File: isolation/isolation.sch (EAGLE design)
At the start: 21 parts, among them IC1 XTLV61048DBVR

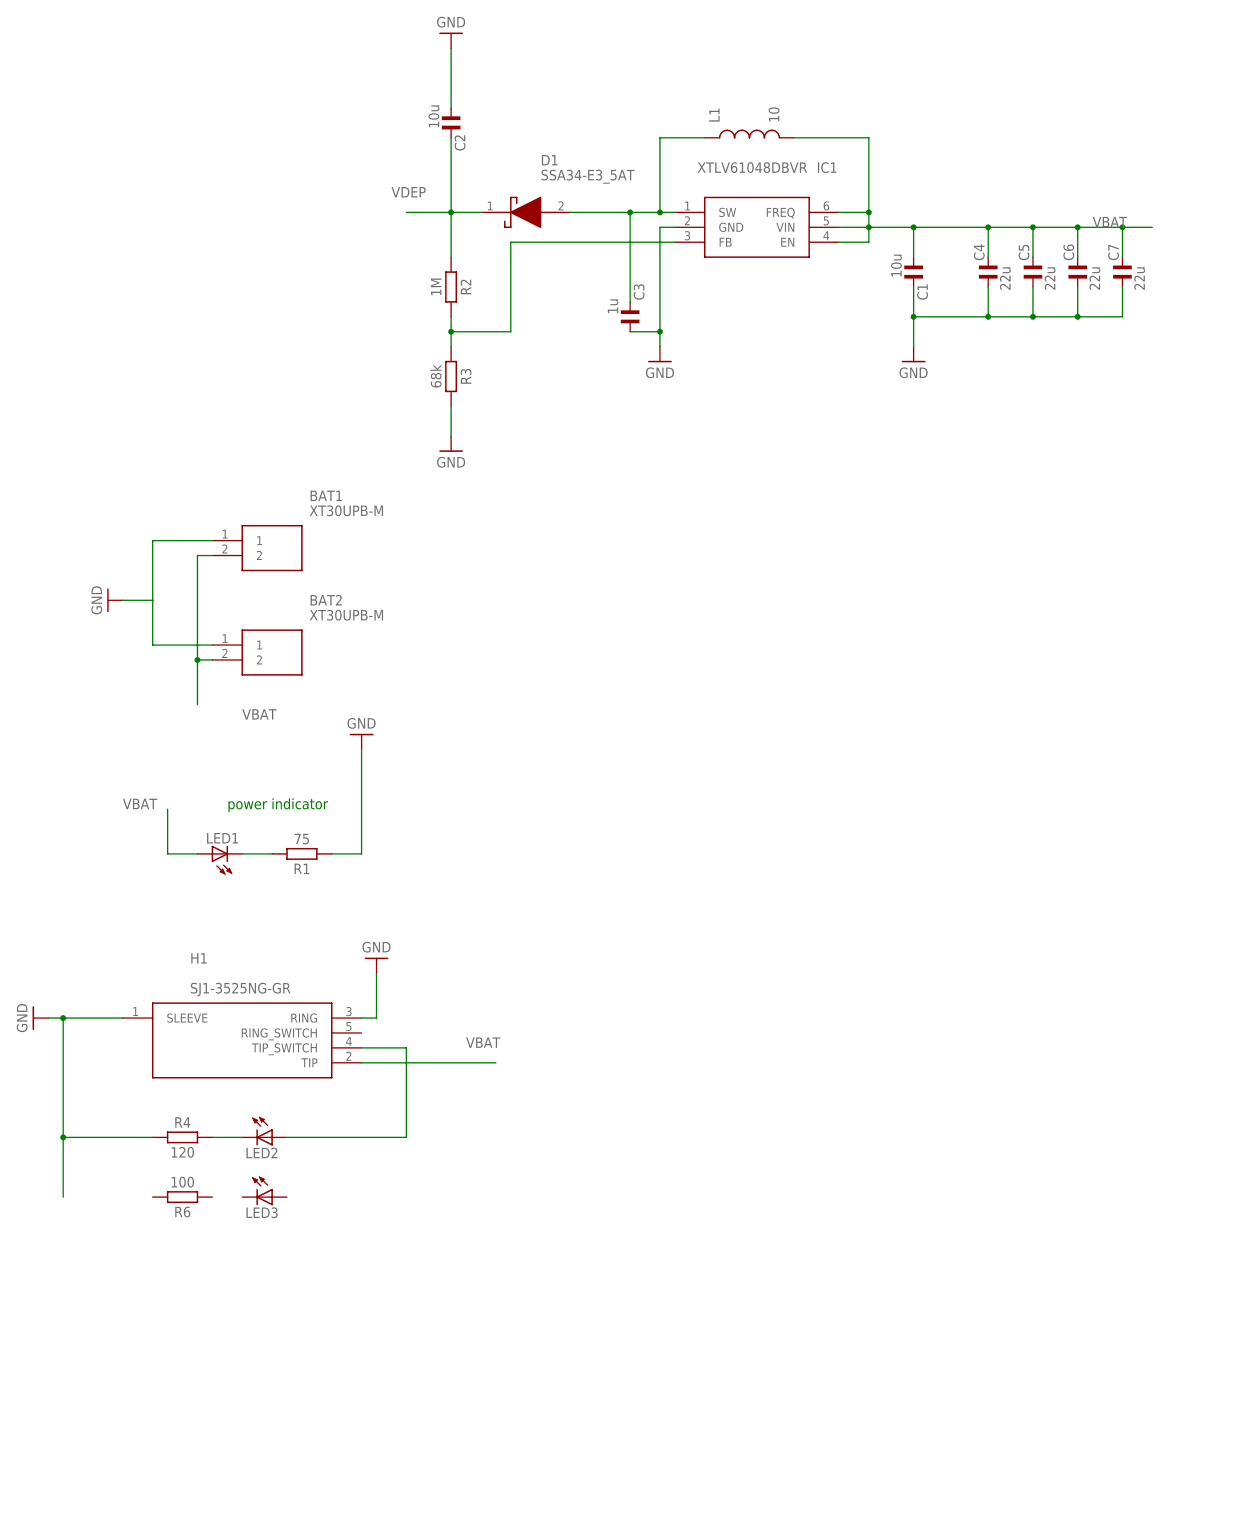
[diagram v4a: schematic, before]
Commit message: headphone jack with inverter
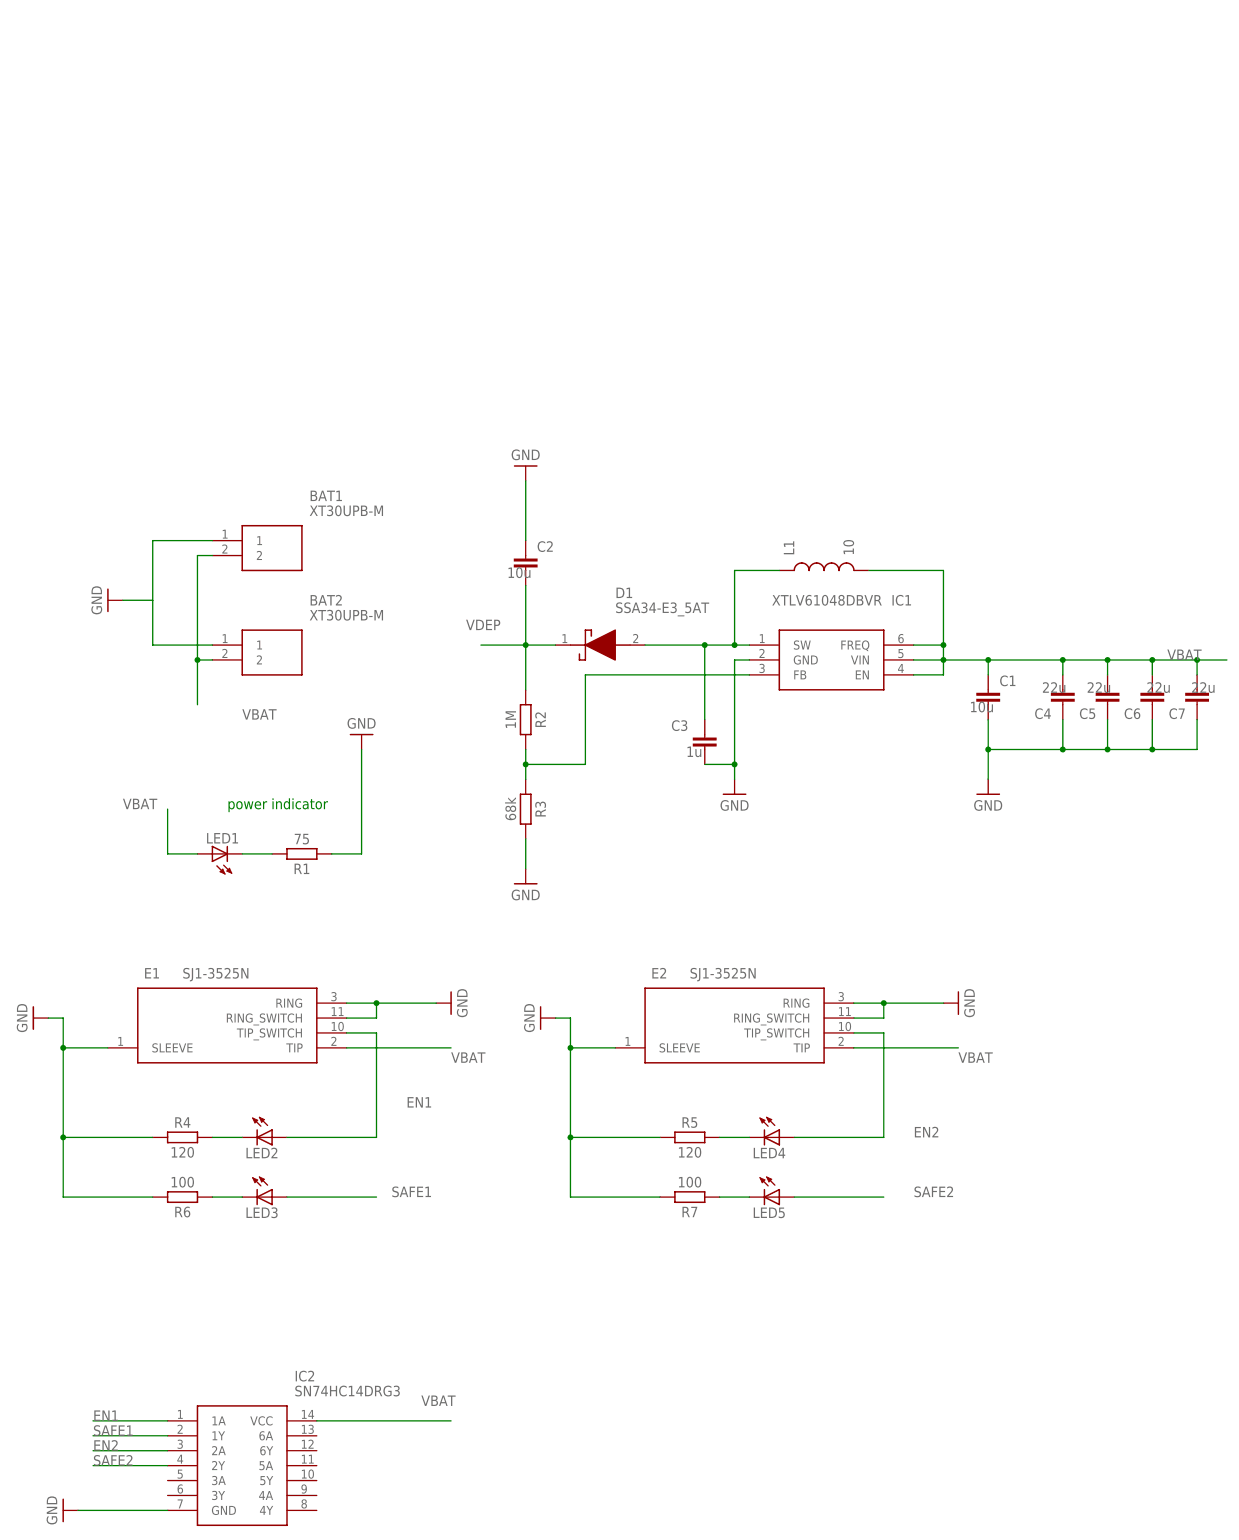
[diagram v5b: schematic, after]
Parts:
- removed H1: SJ1-3525NG-GR, SamacSys_Parts:SJ1-3525NG-GR
- added E1, E2: SJ1-3525N, SamacSys_Parts:SJ1-3525N
- added IC2: SN74HC14DRG3, SamacSys_Parts:SN74HC14DRG3
- added LED4, LED5: (no value), adafruit:LEDCHIPLED_0805
- added R5: 120, Resistor:R_CHIP-0603(1608-METRIC)
- added R7: 100, Resistor:R_CHIP-0603(1608-METRIC)
- C1, C2, C3, C4, C5, C6, C7: device 52101-101-REV-A_v16:RC-MASTER-SMD_C_0603MP -> Capacitor:C_CHIP-0603(1608-METRIC)
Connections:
- new net EN2: E2.TIP_SWITCH, IC2.2A, LED4.A
- new net N$4: LED4.C, R5.2
- new net N$6: LED3.C, R6.1
- new net N$7: LED5.C, R7.1
- new net SAFE1: IC2.1Y, LED3.A
- new net SAFE2: IC2.2Y, LED5.A
- net EN1: now also E1.TIP_SWITCH, IC2.1A; no longer H1.TIP_SWITCH
- net GND: now also E1.RING, E1.RING_SWITCH, E1.SLEEVE, E2.RING, E2.RING_SWITCH, E2.SLEEVE, IC2.GND, R5.1, R6.2, R7.2; no longer H1.RING, H1.SLEEVE
- net VBAT: now also E1.TIP, E2.TIP, IC2.VCC; no longer H1.TIP
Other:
- moved on the sheet: D1, IC1, L1, R2, R3

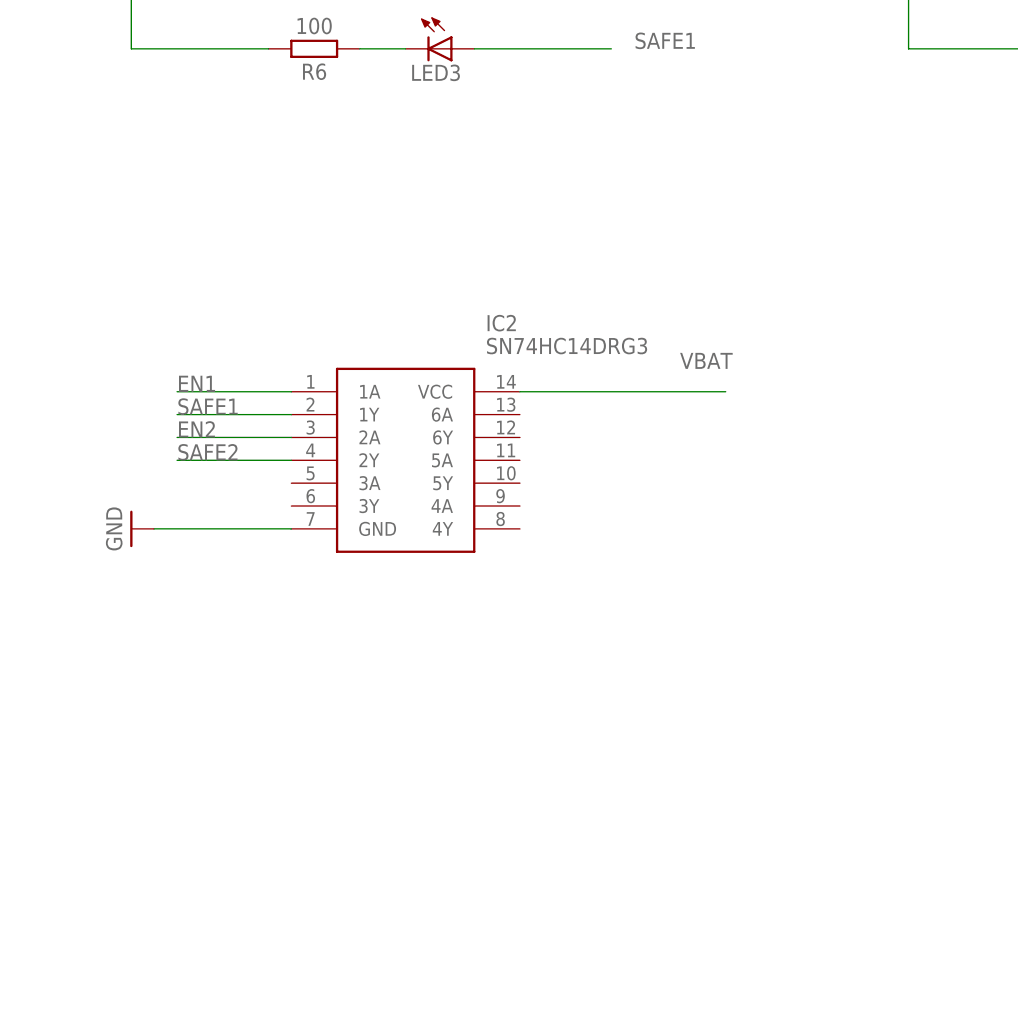
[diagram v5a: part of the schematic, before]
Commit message: jst inputs from flight computers
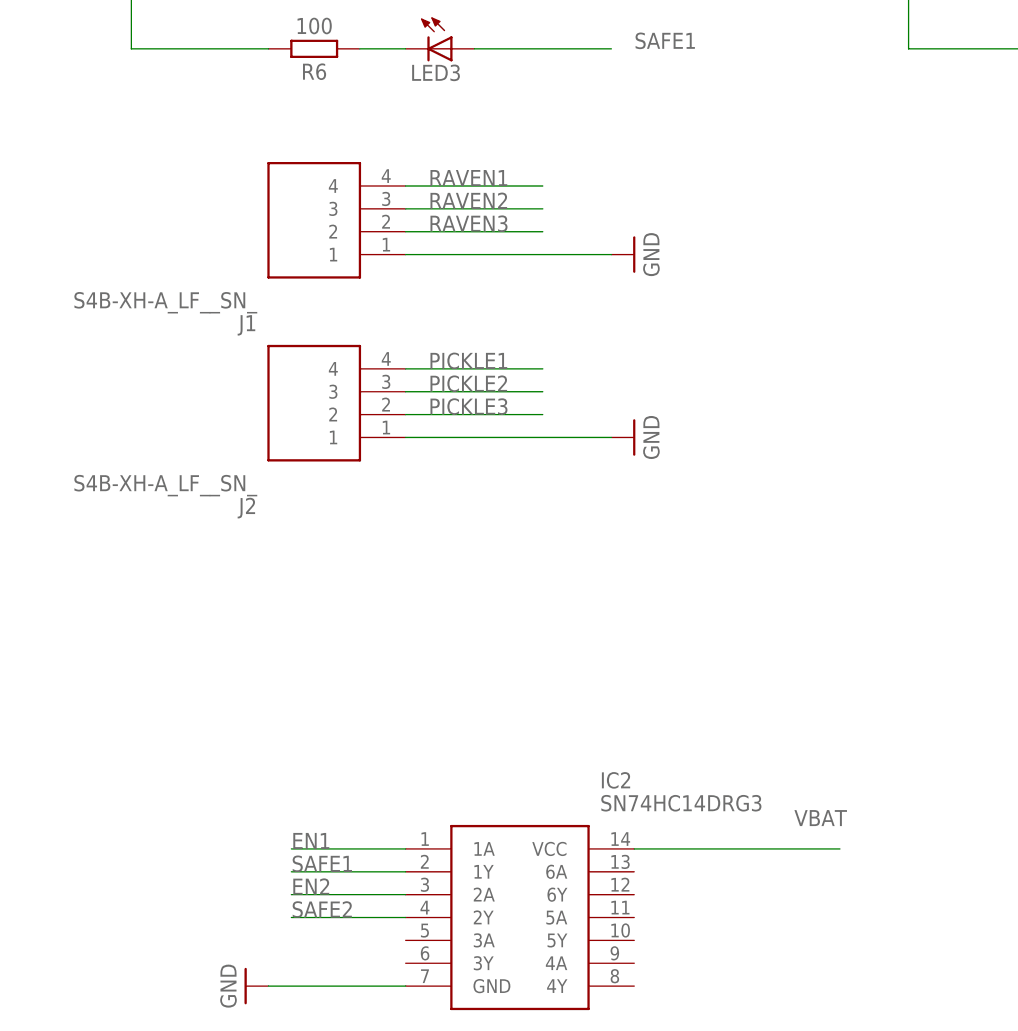
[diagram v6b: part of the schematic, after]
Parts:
- added J1, J2: S4B-XH-A_LF__SN_, SamacSys_Parts:S4B-XH-A_LF__SN_
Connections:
- new net PICKLE1: J2.4
- new net PICKLE2: J2.3
- new net PICKLE3: J2.2
- new net RAVEN1: J1.4
- new net RAVEN2: J1.3
- new net RAVEN3: J1.2
- net GND: now also J1.1, J2.1
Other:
- moved on the sheet: IC2
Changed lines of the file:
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@@
 <part name="E2" library="SamacSys_Parts" deviceset="SJ1-3525N" device=""/>
 <part name="SUPPLY11" library="Power_Symbols" library_urn="urn:adsk.eagle:library:16502351" deviceset="GND-BAR" device="" value="GND"/>
+<part name="J1" library="SamacSys_Parts" deviceset="S4B-XH-A_LF__SN_" device=""/>
+<part name="J2" library="SamacSys_Parts" deviceset="S4B-XH-A_LF__SN_" device=""/>
+<part name="SUPPLY12" library="Power_Symbols" library_urn="urn:adsk.eagle:library:16502351" deviceset="GND-BAR" device="" value="GND"/>
+<part name="SUPPLY13" library="Power_Symbols" library_urn="urn:adsk.eagle:library:16502351" deviceset="GND-BAR" device="" value="GND"/>
 </parts>
 <sheets>
@@
 <attribute name="VALUE" x="60.325" y="-27.94" size="1.778" layer="96" rot="R90" align="center"/>
 </instance>
-<instance part="IC2" gate="G$1" x="10.16" y="-99.06" smashed="yes">
-<attribute name="NAME" x="31.75" y="-91.44" size="1.778" layer="95" align="center-left"/>
-<attribute name="VALUE" x="31.75" y="-93.98" size="1.778" layer="96" align="center-left"/>
-</instance>
-<instance part="SUPPLY9" gate="G$1" x="-7.62" y="-114.3" smashed="yes" rot="R270">
-<attribute name="VALUE" x="-9.525" y="-114.3" size="1.778" layer="96" rot="R270" align="center"/>
+<instance part="IC2" gate="G$1" x="22.86" y="-149.86" smashed="yes">
+<attribute name="NAME" x="44.45" y="-142.24" size="1.778" layer="95" align="center-left"/>
+<attribute name="VALUE" x="44.45" y="-144.78" size="1.778" layer="96" align="center-left"/>
+</instance>
+<instance part="SUPPLY9" gate="G$1" x="5.08" y="-165.1" smashed="yes" rot="R270">
+<attribute name="VALUE" x="3.175" y="-165.1" size="1.778" layer="96" rot="R270" align="center"/>
 </instance>
 <instance part="SUPPLY10" gate="G$1" x="73.66" y="-30.48" smashed="yes" rot="R270">
@@
 <instance part="SUPPLY11" gate="G$1" x="144.78" y="-27.94" smashed="yes" rot="R90">
 <attribute name="VALUE" x="146.685" y="-27.94" size="1.778" layer="96" rot="R90" align="center"/>
+</instance>
+<instance part="J1" gate="G$1" x="22.86" y="-83.82" smashed="yes" rot="R180">
+<attribute name="NAME" x="6.35" y="-91.44" size="1.778" layer="95" rot="R180" align="center-left"/>
+<attribute name="VALUE" x="6.35" y="-88.9" size="1.778" layer="96" rot="R180" align="center-left"/>
+</instance>
+<instance part="J2" gate="G$1" x="22.86" y="-104.14" smashed="yes" rot="R180">
+<attribute name="NAME" x="6.35" y="-111.76" size="1.778" layer="95" rot="R180" align="center-left"/>
+<attribute name="VALUE" x="6.35" y="-109.22" size="1.778" layer="96" rot="R180" align="center-left"/>
+</instance>
+<instance part="SUPPLY12" gate="G$1" x="48.26" y="-104.14" smashed="yes" rot="R90">
+<attribute name="VALUE" x="50.165" y="-104.14" size="1.778" layer="96" rot="R90" align="center"/>
+</instance>
+<instance part="SUPPLY13" gate="G$1" x="48.26" y="-83.82" smashed="yes" rot="R90">
+<attribute name="VALUE" x="50.165" y="-83.82" size="1.778" layer="96" rot="R90" align="center"/>
 </instance>
 </instances>
@@
 <pinref part="IC2" gate="G$1" pin="GND"/>
 <pinref part="SUPPLY9" gate="G$1" pin="GND"/>
-<wire x1="10.16" y1="-114.3" x2="-5.08" y2="-114.3" width="0.1524" layer="91"/>
+<wire x1="22.86" y1="-165.1" x2="7.62" y2="-165.1" width="0.1524" layer="91"/>
 </segment>
 <segment>
@@
 <wire x1="132.08" y1="-30.48" x2="132.08" y2="-27.94" width="0.1524" layer="91"/>
 <junction x="132.08" y="-27.94"/>
+</segment>
+<segment>
+<pinref part="J1" gate="G$1" pin="1"/>
+<wire x1="22.86" y1="-83.82" x2="45.72" y2="-83.82" width="0.1524" layer="91"/>
+<pinref part="SUPPLY13" gate="G$1" pin="GND"/>
+</segment>
+<segment>
+<pinref part="J2" gate="G$1" pin="1"/>
+<wire x1="22.86" y1="-104.14" x2="45.72" y2="-104.14" width="0.1524" layer="91"/>
+<pinref part="SUPPLY12" gate="G$1" pin="GND"/>
 </segment>
 </net>
@@
 <segment>
 <pinref part="IC2" gate="G$1" pin="VCC"/>
-<wire x1="35.56" y1="-99.06" x2="58.42" y2="-99.06" width="0.1524" layer="91"/>
-<label x="53.34" y="-96.52" size="1.778" layer="95"/>
+<wire x1="48.26" y1="-149.86" x2="71.12" y2="-149.86" width="0.1524" layer="91"/>
+<label x="66.04" y="-147.32" size="1.778" layer="95"/>
 </segment>
 <segment>
@@
 <segment>
 <pinref part="IC2" gate="G$1" pin="1A"/>
-<wire x1="10.16" y1="-99.06" x2="-2.54" y2="-99.06" width="0.1524" layer="91"/>
-<label x="-2.54" y="-99.06" size="1.778" layer="95"/>
+<wire x1="22.86" y1="-149.86" x2="10.16" y2="-149.86" width="0.1524" layer="91"/>
+<label x="10.16" y="-149.86" size="1.778" layer="95"/>
 </segment>
 </net>
@@
 <segment>
 <pinref part="IC2" gate="G$1" pin="1Y"/>
-<wire x1="10.16" y1="-101.6" x2="-2.54" y2="-101.6" width="0.1524" layer="91"/>
-<label x="-2.54" y="-101.6" size="1.778" layer="95"/>
+<wire x1="22.86" y1="-152.4" x2="10.16" y2="-152.4" width="0.1524" layer="91"/>
+<label x="10.16" y="-152.4" size="1.778" layer="95"/>
 </segment>
 <segment>
@@
 <segment>
 <pinref part="IC2" gate="G$1" pin="2A"/>
-<wire x1="10.16" y1="-104.14" x2="-2.54" y2="-104.14" width="0.1524" layer="91"/>
-<label x="-2.54" y="-104.14" size="1.778" layer="95"/>
+<wire x1="22.86" y1="-154.94" x2="10.16" y2="-154.94" width="0.1524" layer="91"/>
+<label x="10.16" y="-154.94" size="1.778" layer="95"/>
 </segment>
 <segment>
@@
 <segment>
 <pinref part="IC2" gate="G$1" pin="2Y"/>
-<wire x1="10.16" y1="-106.68" x2="-2.54" y2="-106.68" width="0.1524" layer="91"/>
-<label x="-2.54" y="-106.68" size="1.778" layer="95"/>
+<wire x1="22.86" y1="-157.48" x2="10.16" y2="-157.48" width="0.1524" layer="91"/>
+<label x="10.16" y="-157.48" size="1.778" layer="95"/>
 </segment>
 <segment>
@@
 </segment>
 </net>
+<net name="PICKLE3" class="0">
+<segment>
+<pinref part="J2" gate="G$1" pin="2"/>
+<wire x1="22.86" y1="-101.6" x2="38.1" y2="-101.6" width="0.1524" layer="91"/>
+<label x="25.4" y="-101.6" size="1.778" layer="95"/>
+</segment>
+</net>
+<net name="PICKLE2" class="0">
+<segment>
+<pinref part="J2" gate="G$1" pin="3"/>
+<wire x1="22.86" y1="-99.06" x2="38.1" y2="-99.06" width="0.1524" layer="91"/>
+<label x="25.4" y="-99.06" size="1.778" layer="95"/>
+</segment>
+</net>
+<net name="PICKLE1" class="0">
+<segment>
+<pinref part="J2" gate="G$1" pin="4"/>
+<wire x1="22.86" y1="-96.52" x2="38.1" y2="-96.52" width="0.1524" layer="91"/>
+<label x="25.4" y="-96.52" size="1.778" layer="95"/>
+</segment>
+</net>
+<net name="RAVEN3" class="0">
+<segment>
+<pinref part="J1" gate="G$1" pin="2"/>
+<wire x1="22.86" y1="-81.28" x2="38.1" y2="-81.28" width="0.1524" layer="91"/>
+<label x="25.4" y="-81.28" size="1.778" layer="95"/>
+</segment>
+</net>
+<net name="RAVEN2" class="0">
+<segment>
+<pinref part="J1" gate="G$1" pin="3"/>
+<wire x1="22.86" y1="-78.74" x2="38.1" y2="-78.74" width="0.1524" layer="91"/>
+<label x="25.4" y="-78.74" size="1.778" layer="95"/>
+</segment>
+</net>
+<net name="RAVEN1" class="0">
+<segment>
+<pinref part="J1" gate="G$1" pin="4"/>
+<wire x1="22.86" y1="-76.2" x2="38.1" y2="-76.2" width="0.1524" layer="91"/>
+<label x="25.4" y="-76.2" size="1.778" layer="95"/>
+</segment>
+</net>

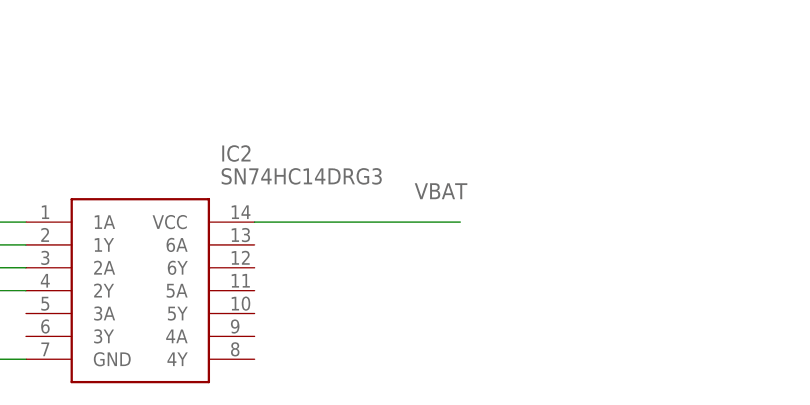
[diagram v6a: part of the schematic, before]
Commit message: invert raven inputs
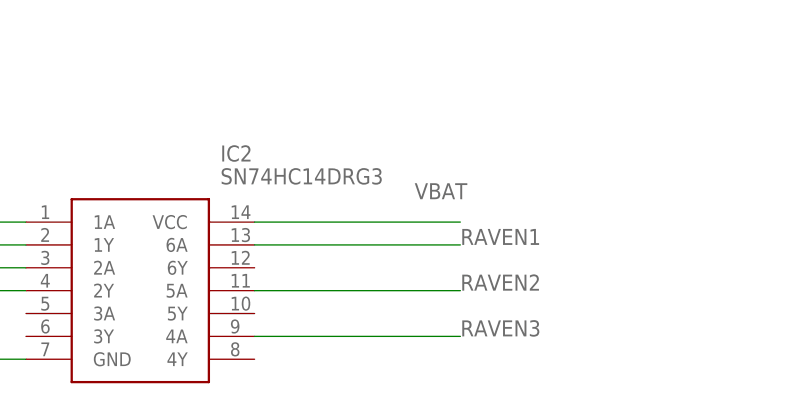
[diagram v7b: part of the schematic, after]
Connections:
- net RAVEN1: now also IC2.6A
- net RAVEN2: now also IC2.5A
- net RAVEN3: now also IC2.4A
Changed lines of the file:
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@@
 <label x="25.4" y="-81.28" size="1.778" layer="95"/>
+</segment>
+<segment>
+<pinref part="IC2" gate="G$1" pin="4A"/>
+<wire x1="48.26" y1="-162.56" x2="71.12" y2="-162.56" width="0.1524" layer="91"/>
+<label x="71.12" y="-162.56" size="1.778" layer="95"/>
 </segment>
 </net>
@@
 <label x="25.4" y="-78.74" size="1.778" layer="95"/>
 </segment>
+<segment>
+<pinref part="IC2" gate="G$1" pin="5A"/>
+<wire x1="48.26" y1="-157.48" x2="71.12" y2="-157.48" width="0.1524" layer="91"/>
+<label x="71.12" y="-157.48" size="1.778" layer="95"/>
+</segment>
 </net>
 <net name="RAVEN1" class="0">
@@
 <label x="25.4" y="-76.2" size="1.778" layer="95"/>
 </segment>
+<segment>
+<pinref part="IC2" gate="G$1" pin="6A"/>
+<wire x1="48.26" y1="-152.4" x2="71.12" y2="-152.4" width="0.1524" layer="91"/>
+<label x="71.12" y="-152.4" size="1.778" layer="95"/>
+</segment>
 </net>
